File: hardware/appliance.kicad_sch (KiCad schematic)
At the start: 0 parts

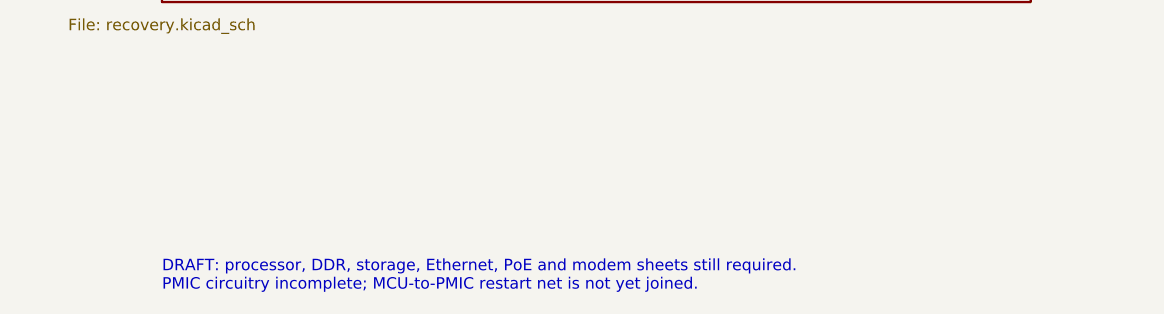
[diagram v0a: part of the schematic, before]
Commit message: Connect supervisor restart GPIO to PMIC power-on sink
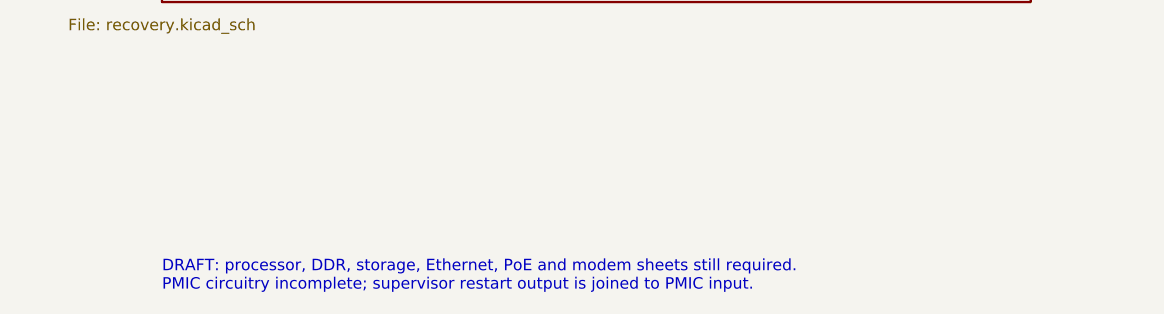
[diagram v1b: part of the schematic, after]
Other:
- note added: "DRAFT: processor, DDR, storage, Ethernet, PoE and modem sheets still required. PMIC circuitry incomplete; supervisor restart output is joined to PMIC input."
- note removed: "DRAFT: processor, DDR, storage, Ethernet, PoE and modem sheets still required. PMIC circuitry incomplete; MCU-to-PMIC restart net is not yet joined."

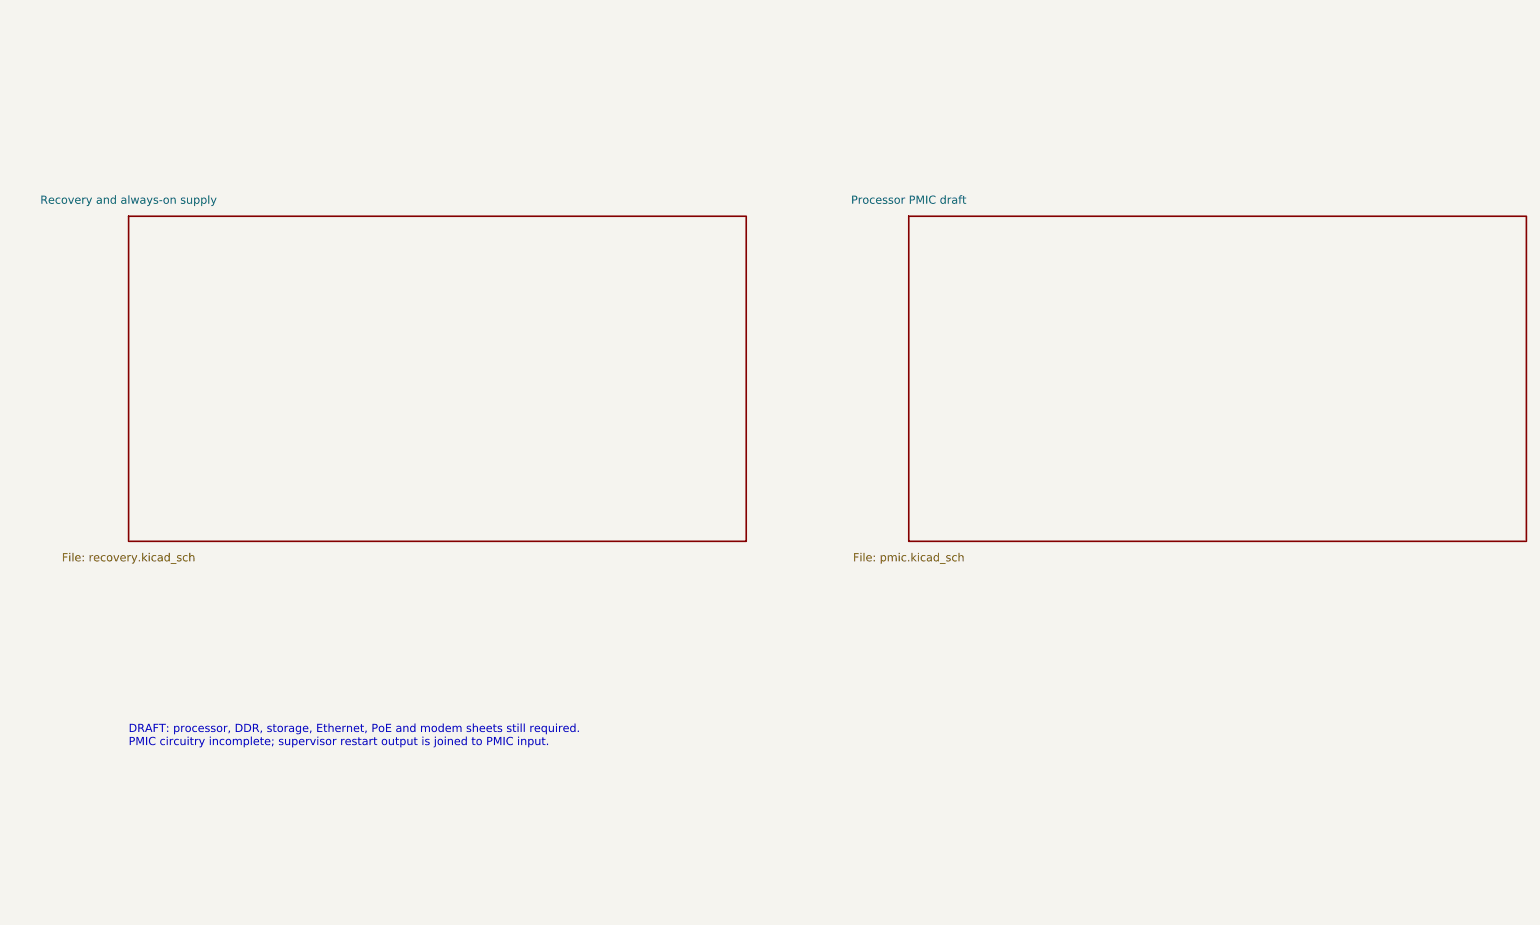
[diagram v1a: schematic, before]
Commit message: Integrate main 3.3 V regulator and PMIC supply nets
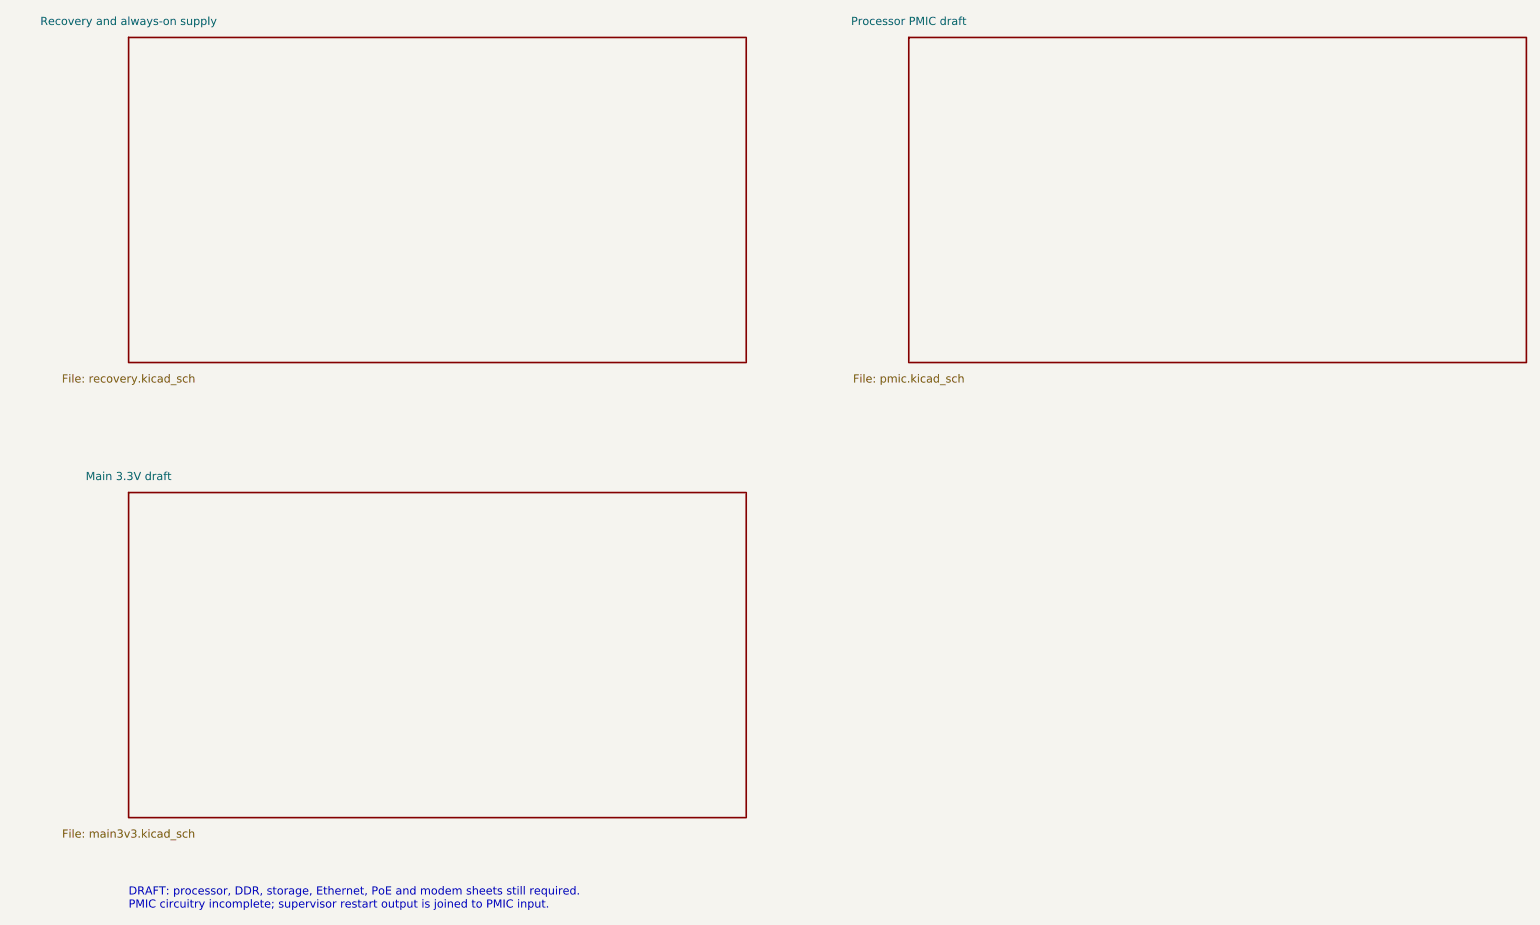
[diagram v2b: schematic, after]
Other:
- added sheet Main 3.3V draft (main3v3.kicad_sch)

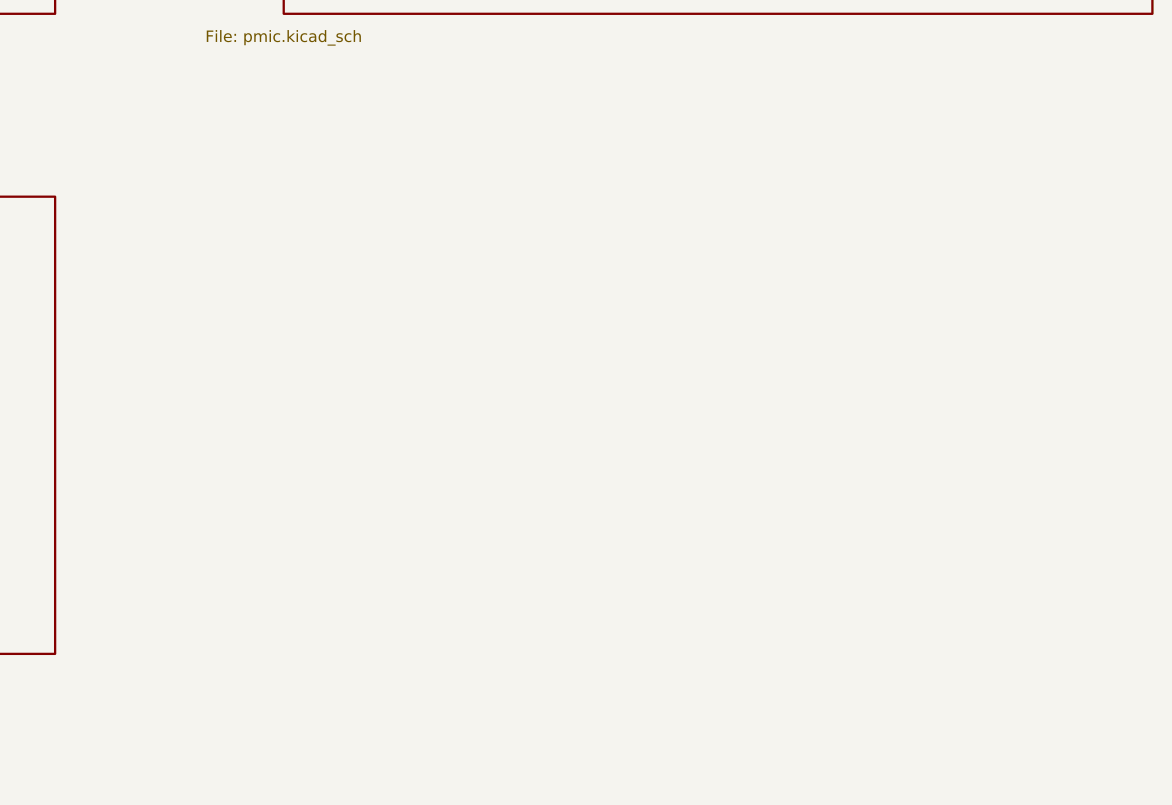
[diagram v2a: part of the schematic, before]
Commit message: Capture main 5 V regulator mode and feedback in appliance draft
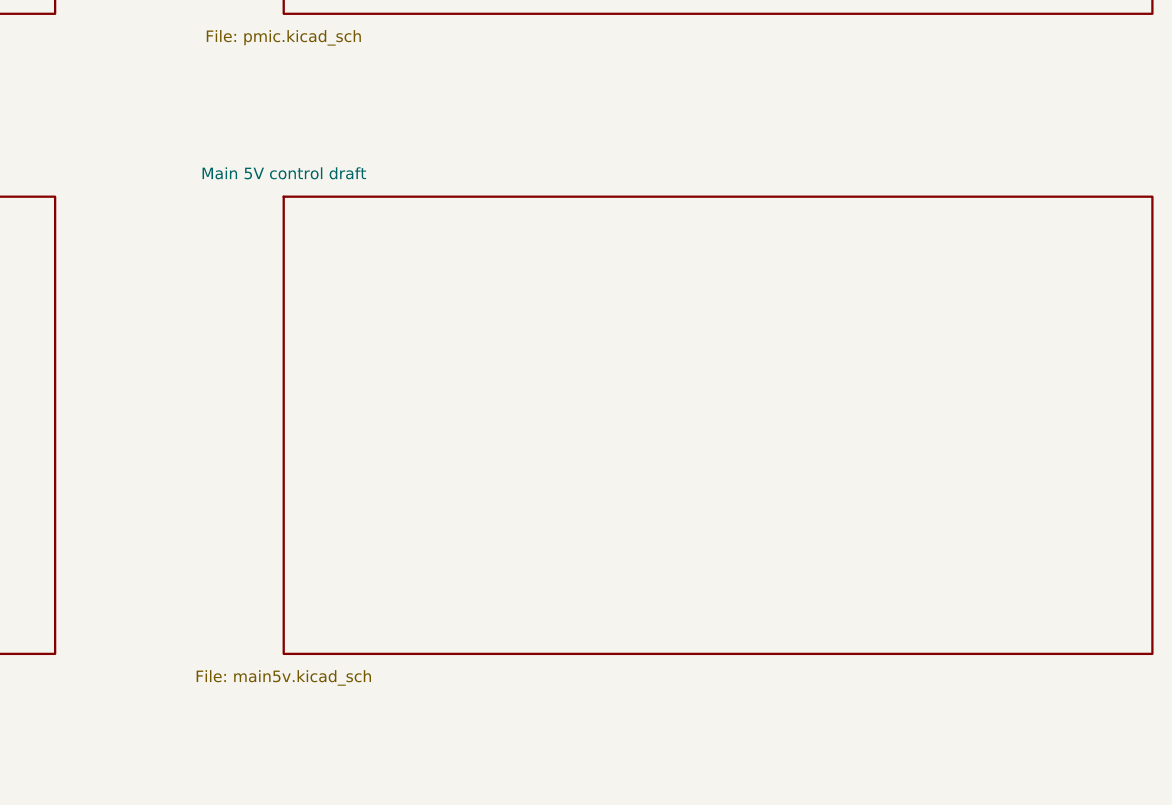
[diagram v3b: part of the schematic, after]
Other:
- added sheet Main 5V control draft (main5v.kicad_sch)

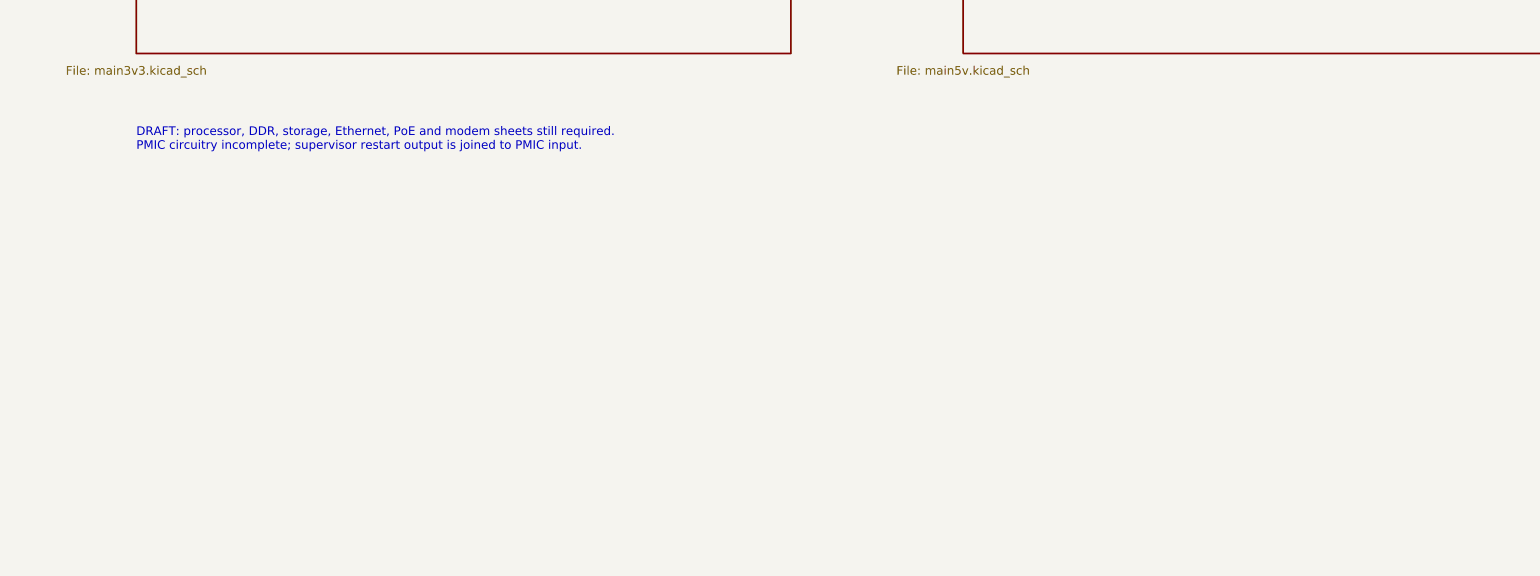
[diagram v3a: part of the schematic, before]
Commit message: Integrate processor draft and PMIC controls into appliance hierarchy
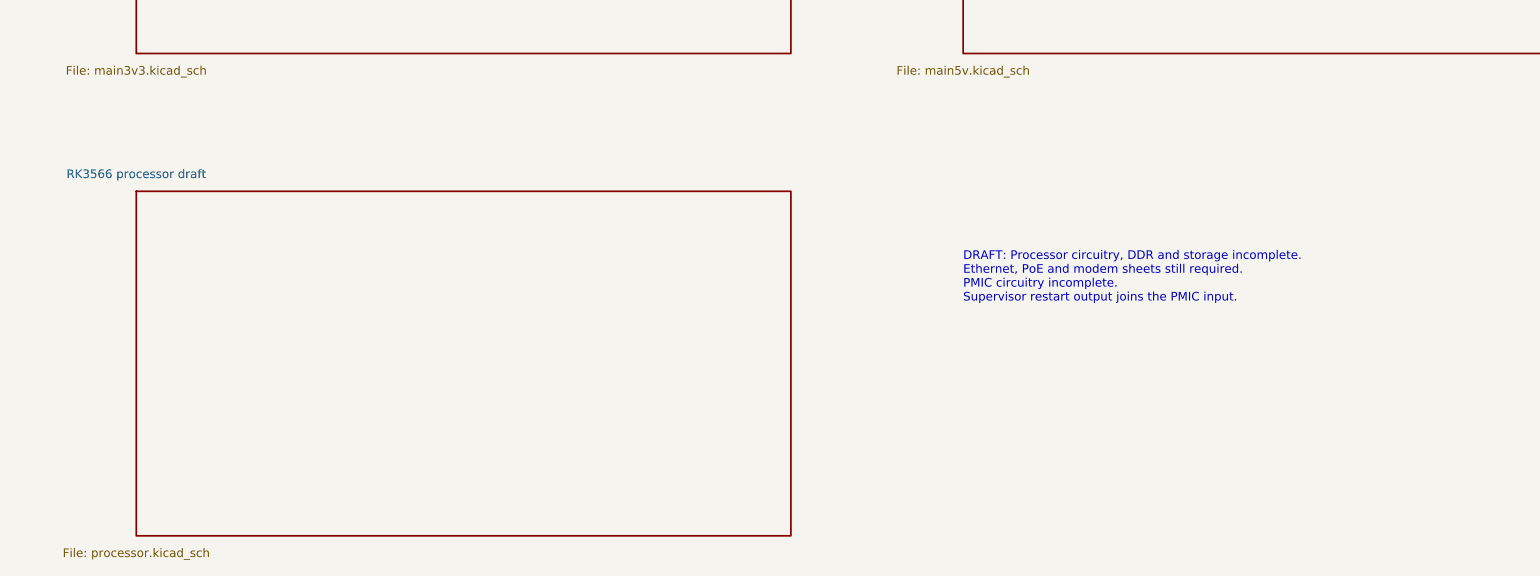
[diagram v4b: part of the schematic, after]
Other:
- added sheet RK3566 processor draft (processor.kicad_sch)
- note added: "DRAFT: Processor circuitry, DDR and storage incomplete. Ethernet, PoE and modem sheets still required. PMIC circuitry incomplete. Supervisor restart output joins the PMIC input."
- note removed: "DRAFT: processor, DDR, storage, Ethernet, PoE and modem sheets still required. PMIC circuitry incomplete; supervisor restart output is joined to PMIC input."

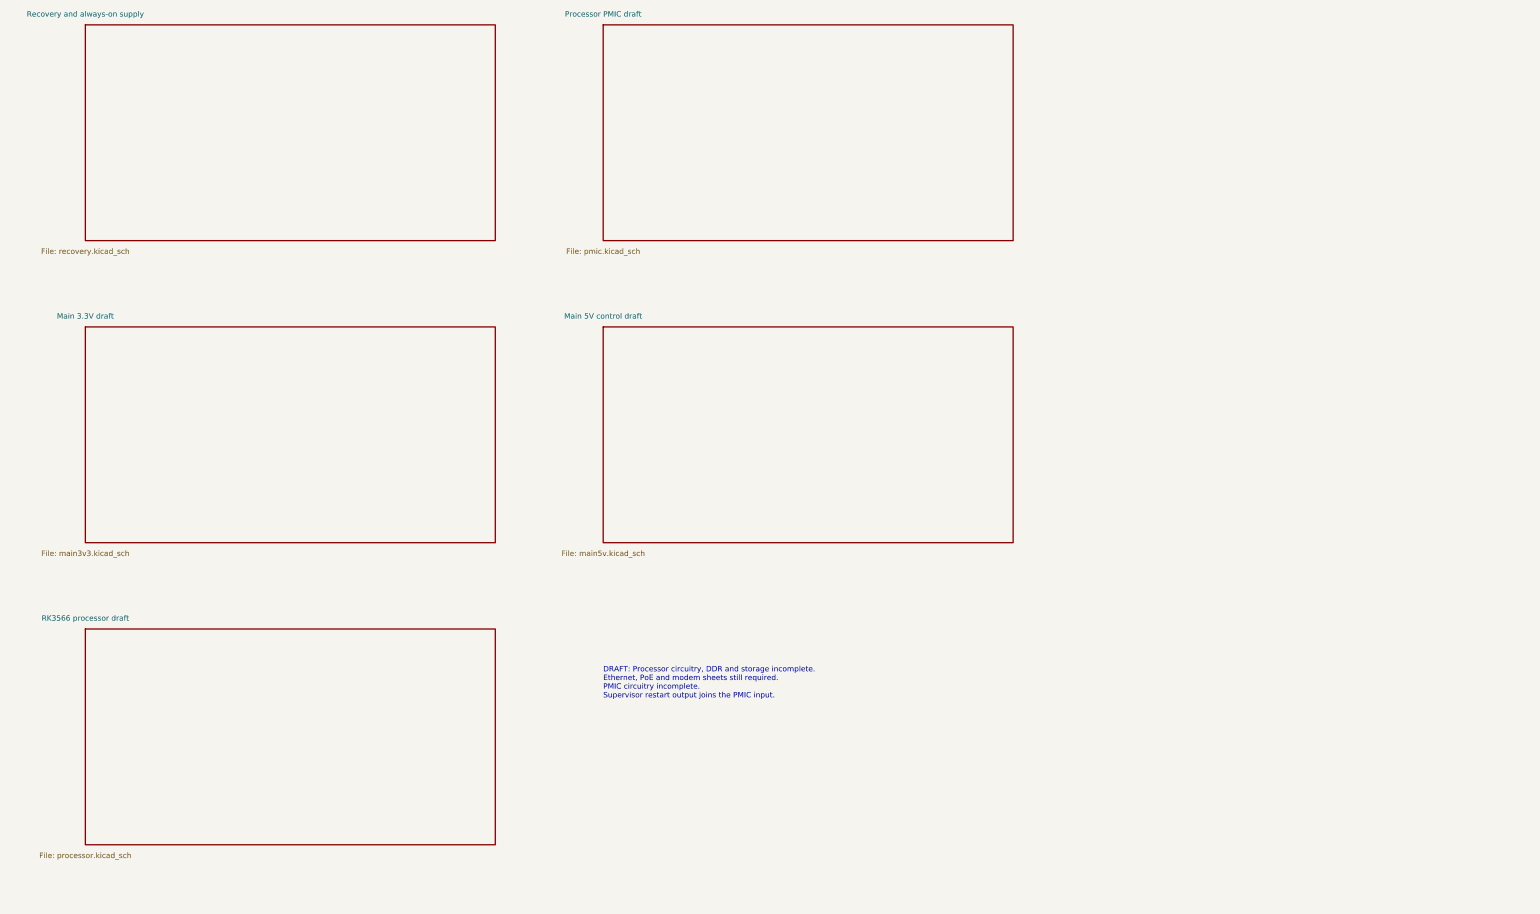
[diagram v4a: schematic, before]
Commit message: Capture separate USB analog supply filters in appliance schematic
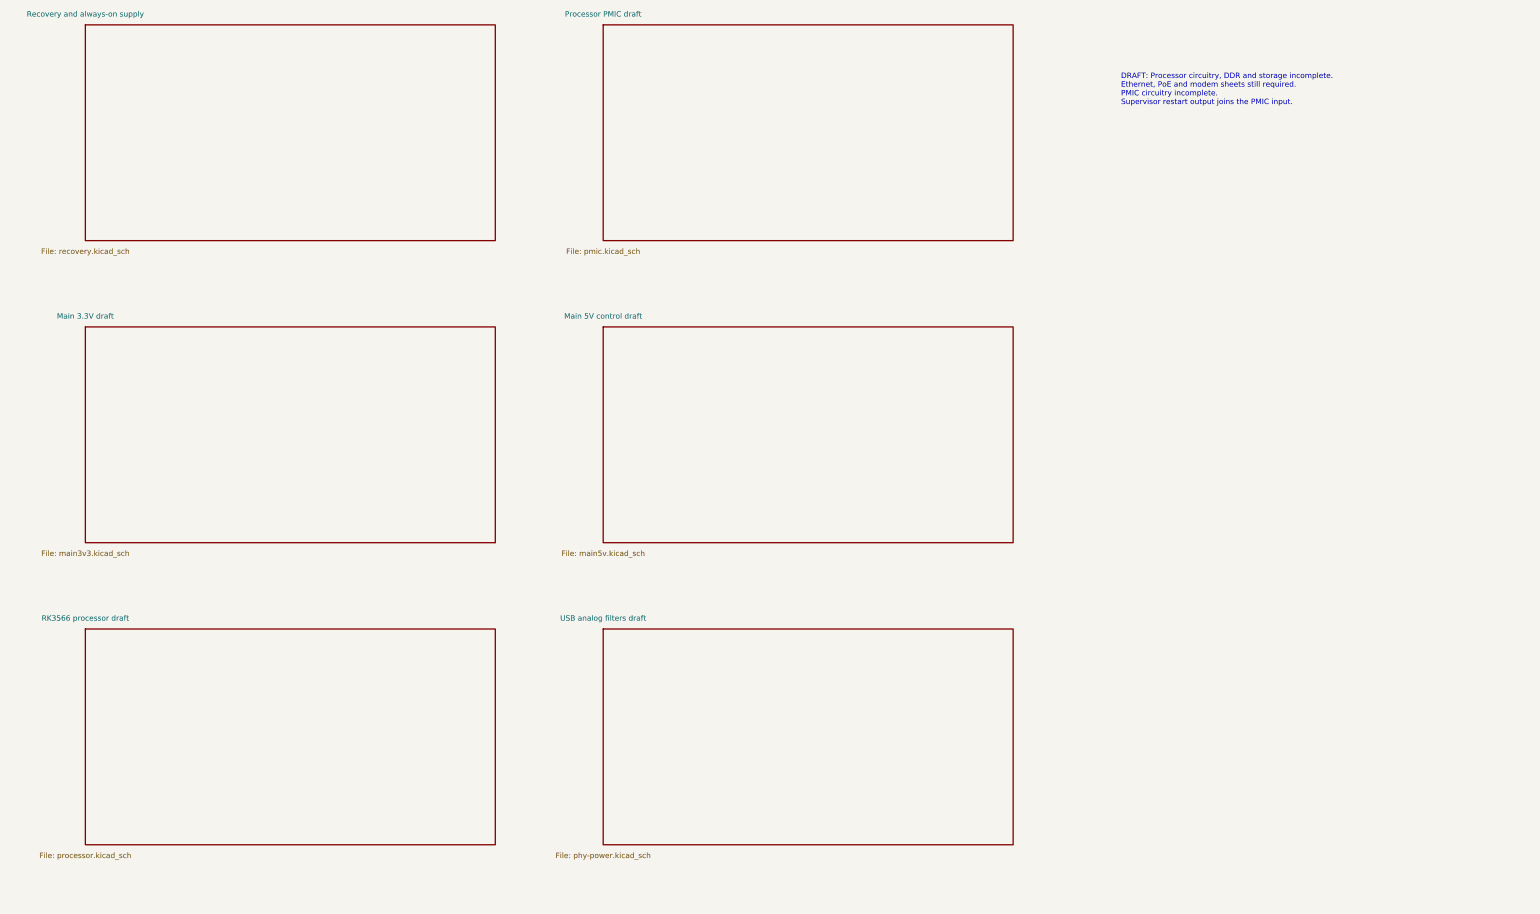
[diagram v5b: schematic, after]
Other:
- added sheet USB analog filters draft (phy-power.kicad_sch)
